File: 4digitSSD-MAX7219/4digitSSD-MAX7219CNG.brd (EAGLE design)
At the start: 70.8 x 49.5 mm, 5 parts, among them IC1 MAX7219CNG

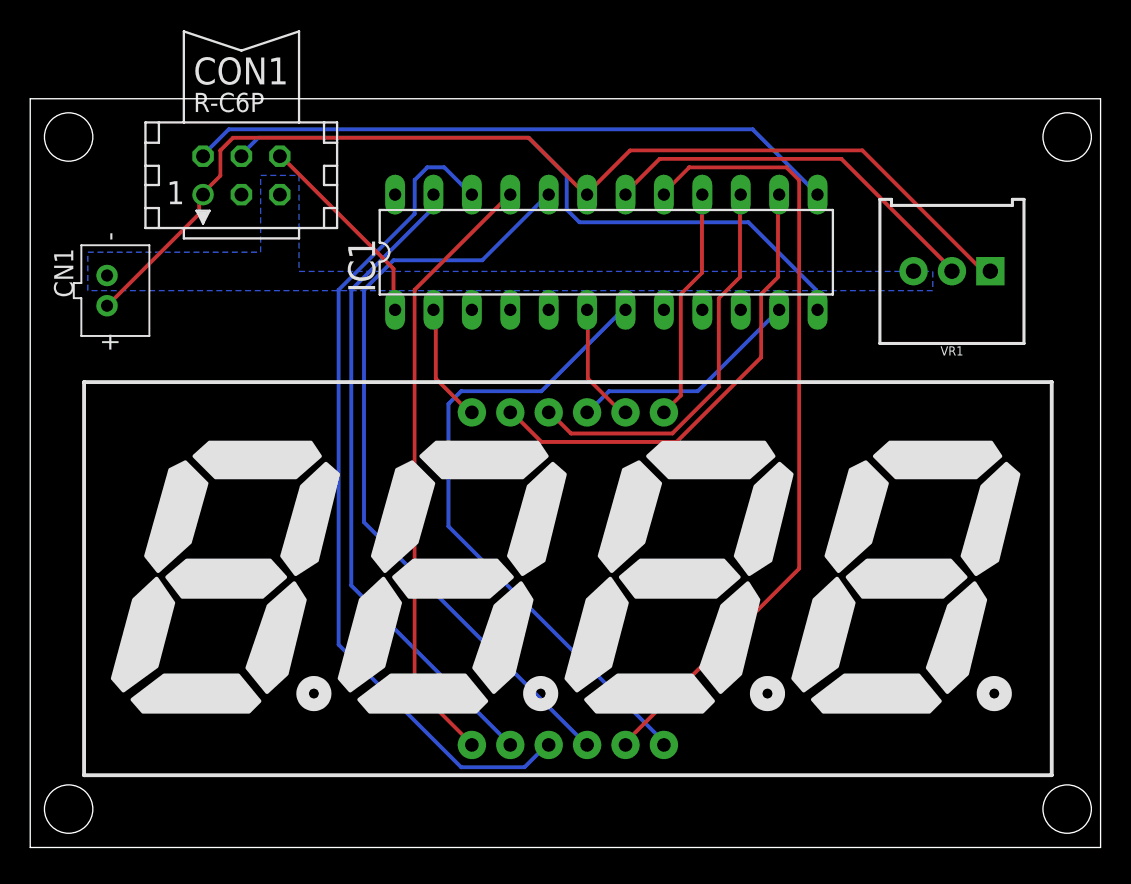
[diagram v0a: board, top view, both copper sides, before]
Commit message: REV 20170118A
slight routing changes. Added power supply filter capacitor.
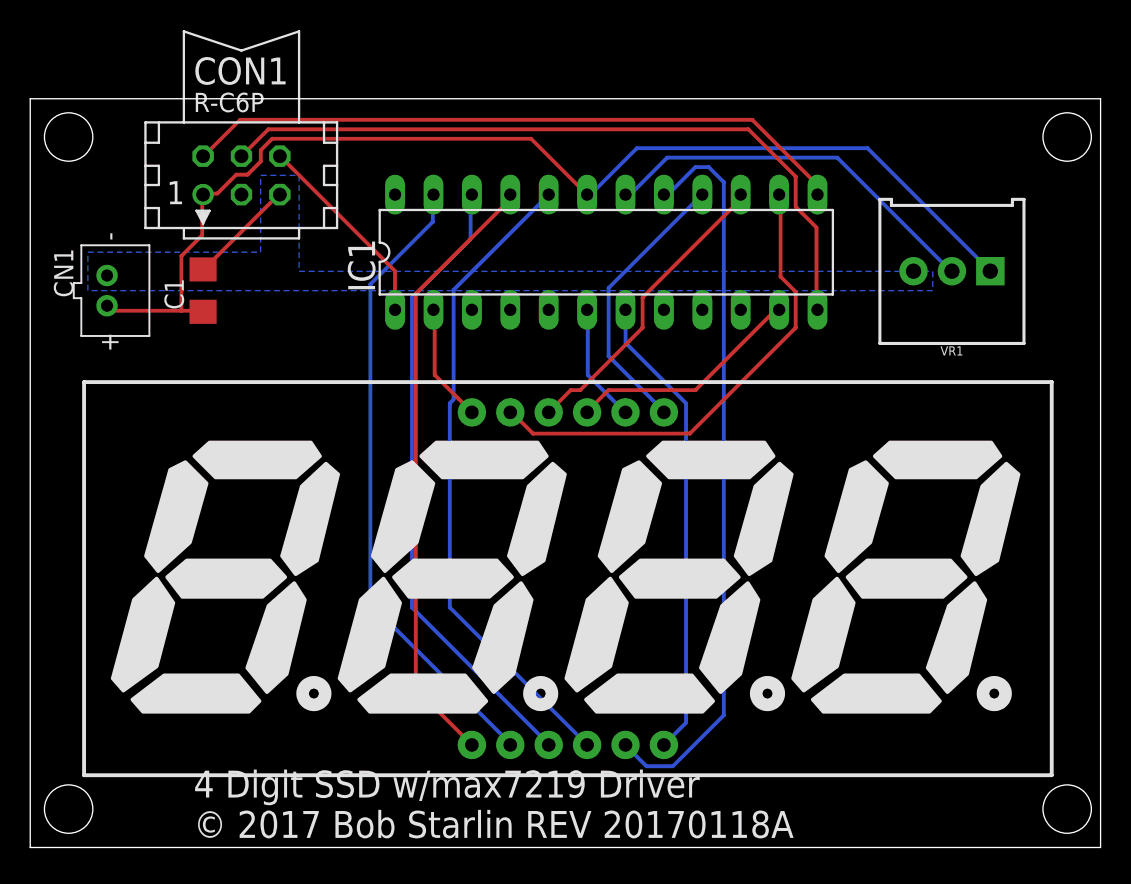
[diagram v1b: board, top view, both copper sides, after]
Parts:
- added C1: .1uF, rcl:C1206
- CN1: value (none) -> Aux PWR
- CON1: value (none) -> uC CONN
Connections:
- removed net D5: IC1.3
- removed net D6: IC1.10
- removed net D7: IC1.5
- removed net D8: IC1.8
- removed net DOUT: IC1.24
- net GND: now also C1.2
- net VCC: now also C1.1
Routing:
- net DP: track 55.5 -> 41.8 mm
- net D4: track 42.7 -> 31.0 mm
- net C: track 51.0 -> 42.9 mm
- net GND: track 0.34 -> 7.69 mm
- net F: track 26.4 -> 20.1 mm
- net VCC: track 70.8 -> 75.0 mm
- net G: track 52.2 -> 48.9 mm
- net B: track 15.4 -> 18.5 mm
- net LOAD: track 45.4 -> 48.1 mm
- net D: track 43.0 -> 42.0 mm
- net CLK: track 43.2 -> 44.0 mm
- net A: track 31.0 -> 31.8 mm
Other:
- board text added: "4 Digit SSD w/max7219 Driver © 2017 Bob Starlin REV 20170118A"
